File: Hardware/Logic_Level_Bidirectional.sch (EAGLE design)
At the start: 17 parts, among them Q1 BSS138, Q2 BSS138, Q3 BSS138, Q4 BSS138

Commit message: Updated Schematic Frame
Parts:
- removed CC_TEXT1: CREATIVE_COMMONS, SparkFun-Aesthetics:CREATIVE_COMMONS
- JP3, JP4: device SparkFun:FIDUCIALUFIDUCIAL -> SparkFun-Aesthetics:FIDUCIALUFIDUCIAL
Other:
- note added: "Patrick Alberts"
- note removed: "Nathan Seidle"
- note removed: "Rev V13 by Patrick Alberts"
- note removed: "Spark Fun Electronics"
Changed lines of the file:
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@@
 </classes>
 <parts>
-<part name="FRAME1" library="SparkFun" deviceset="FRAME-LETTER" device=""/>
 <part name="Q2" library="SparkFun" deviceset="MOSFET-NCHANNEL" device="SMD" value="BSS138"/>
 <part name="R6" library="SparkFun" deviceset="RESISTOR" device="0603-RES" value="10K"/>
@@
 <part name="JP1" library="SparkFun" deviceset="M06" device="SIP"/>
 <part name="JP2" library="SparkFun" deviceset="M06" device="SIP"/>
-<part name="JP3" library="SparkFun" deviceset="FIDUCIAL" device="UFIDUCIAL"/>
-<part name="JP4" library="SparkFun" deviceset="FIDUCIAL" device="UFIDUCIAL"/>
-<part name="CC_TEXT1" library="SparkFun-Aesthetics" deviceset="CREATIVE_COMMONS" device=""/>
 <part name="Q3" library="SparkFun" deviceset="MOSFET-NCHANNEL" device="SMD" value="BSS138"/>
 <part name="R2" library="SparkFun" deviceset="RESISTOR" device="0603-RES" value="10K"/>
@@
 <part name="P+5" library="SparkFun" deviceset="VCC" device="" value="LV"/>
 <part name="P+6" library="SparkFun" deviceset="VCC" device="" value="HV"/>
+<part name="FRAME1" library="SparkFun-Aesthetics" deviceset="FRAME-LETTER" device=""/>
+<part name="JP3" library="SparkFun-Aesthetics" deviceset="FIDUCIAL" device="UFIDUCIAL"/>
+<part name="JP4" library="SparkFun-Aesthetics" deviceset="FIDUCIAL" device="UFIDUCIAL"/>
 </parts>
 <sheets>
@@
 <wire x1="124.46" y1="185.42" x2="127" y2="185.42" width="0.2032" layer="95" style="longdash"/>
 <wire x1="127" y1="185.42" x2="127" y2="121.92" width="0.2032" layer="95" style="longdash"/>
-<text x="154.94" y="27.94" size="2.54" layer="94">Spark Fun Electronics</text>
 <text x="48.26" y="170.18" size="3.302" layer="95">Channel 1</text>
 <text x="175.26" y="170.18" size="3.302" layer="95">Channel 2</text>
 <text x="169.672" y="104.394" size="3.302" layer="95">High Voltage</text>
 <text x="50.546" y="105.41" size="3.302" layer="95">Low Voltage</text>
-<text x="17.78" y="5.08" size="1.778" layer="97" font="vector">Nathan Seidle </text>
-<text x="40.64" y="5.08" size="1.778" layer="97" font="vector">Rev V13 by Patrick Alberts</text>
-<text x="238.76" y="7.62" size="2.54" layer="94">V01</text>
+<text x="241.3" y="48.26" size="2.54" layer="94">V01</text>
+<text x="166.624" y="52.324" size="2.54" layer="94">Patrick Alberts</text>
 </plain>
 <instances>
-<instance part="FRAME1" gate="G$1" x="0" y="0"/>
-<instance part="FRAME1" gate="G$2" x="147.32" y="0"/>
 <instance part="Q2" gate="G$1" x="162.56" y="137.16" smashed="yes" rot="R270">
 <attribute name="NAME" x="158.75" y="141.986" size="1.778" layer="95"/>
@@
 <attribute name="VALUE" x="193.04" y="101.6" size="1.778" layer="96" rot="R180"/>
 </instance>
-<instance part="JP3" gate="G$1" x="205.74" y="27.94"/>
-<instance part="JP4" gate="G$1" x="205.74" y="33.02"/>
-<instance part="CC_TEXT1" gate="G$1" x="5.08" y="5.08"/>
 <instance part="Q3" gate="G$1" x="78.74" y="137.16" smashed="yes" rot="R270">
 <attribute name="NAME" x="74.93" y="141.986" size="1.778" layer="95"/>
@@
 <instance part="P+5" gate="1" x="198.12" y="154.94"/>
 <instance part="P+6" gate="1" x="213.36" y="154.94"/>
+<instance part="FRAME1" gate="G$1" x="0" y="40.64"/>
+<instance part="FRAME1" gate="G$2" x="147.32" y="40.64"/>
+<instance part="JP3" gate="G$1" x="243.84" y="73.66"/>
+<instance part="JP4" gate="G$1" x="243.84" y="68.58"/>
 </instances>
 <busses>

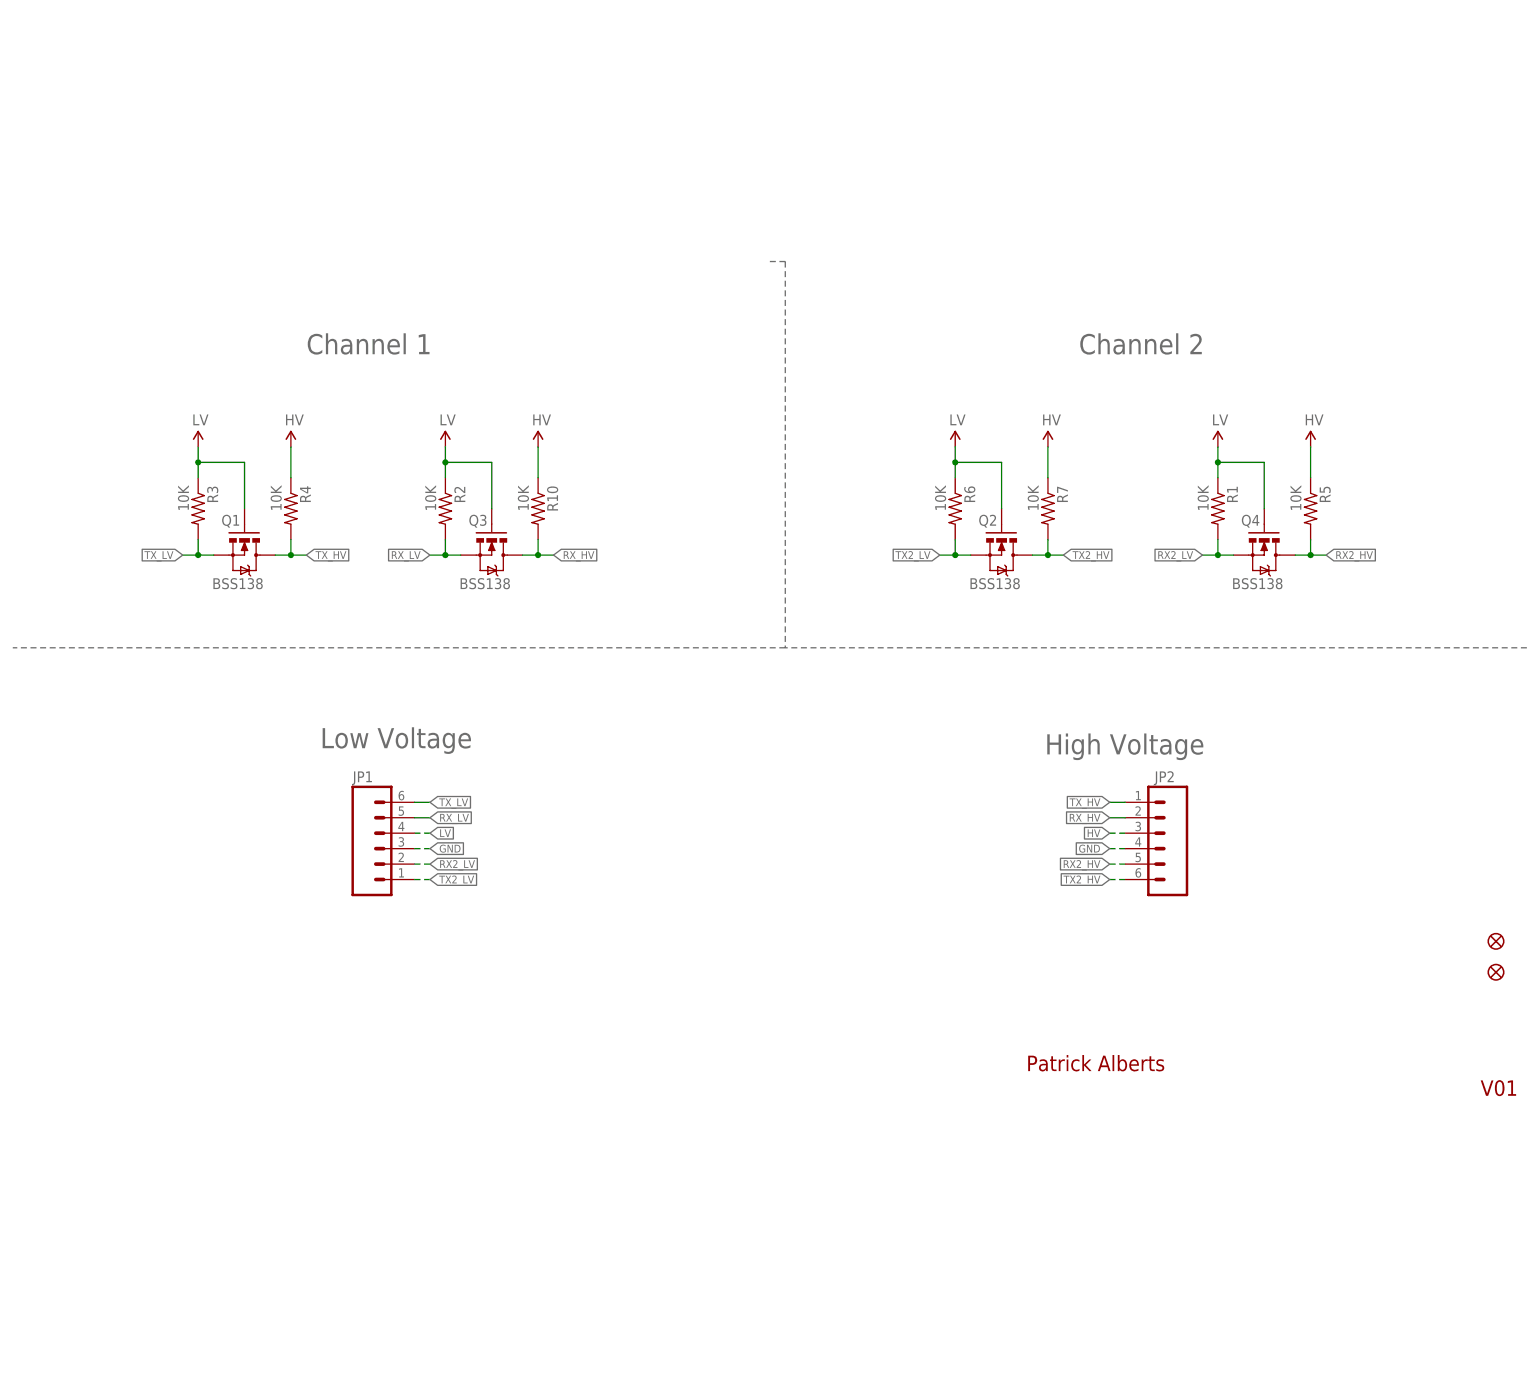
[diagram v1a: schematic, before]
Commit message: Silk Change, Schematic Change
Added deviding lines for HV/LV passages and change silk names as well
from RXO/TXO to HV1 LV2...etc as well as cleaned up the schematic.
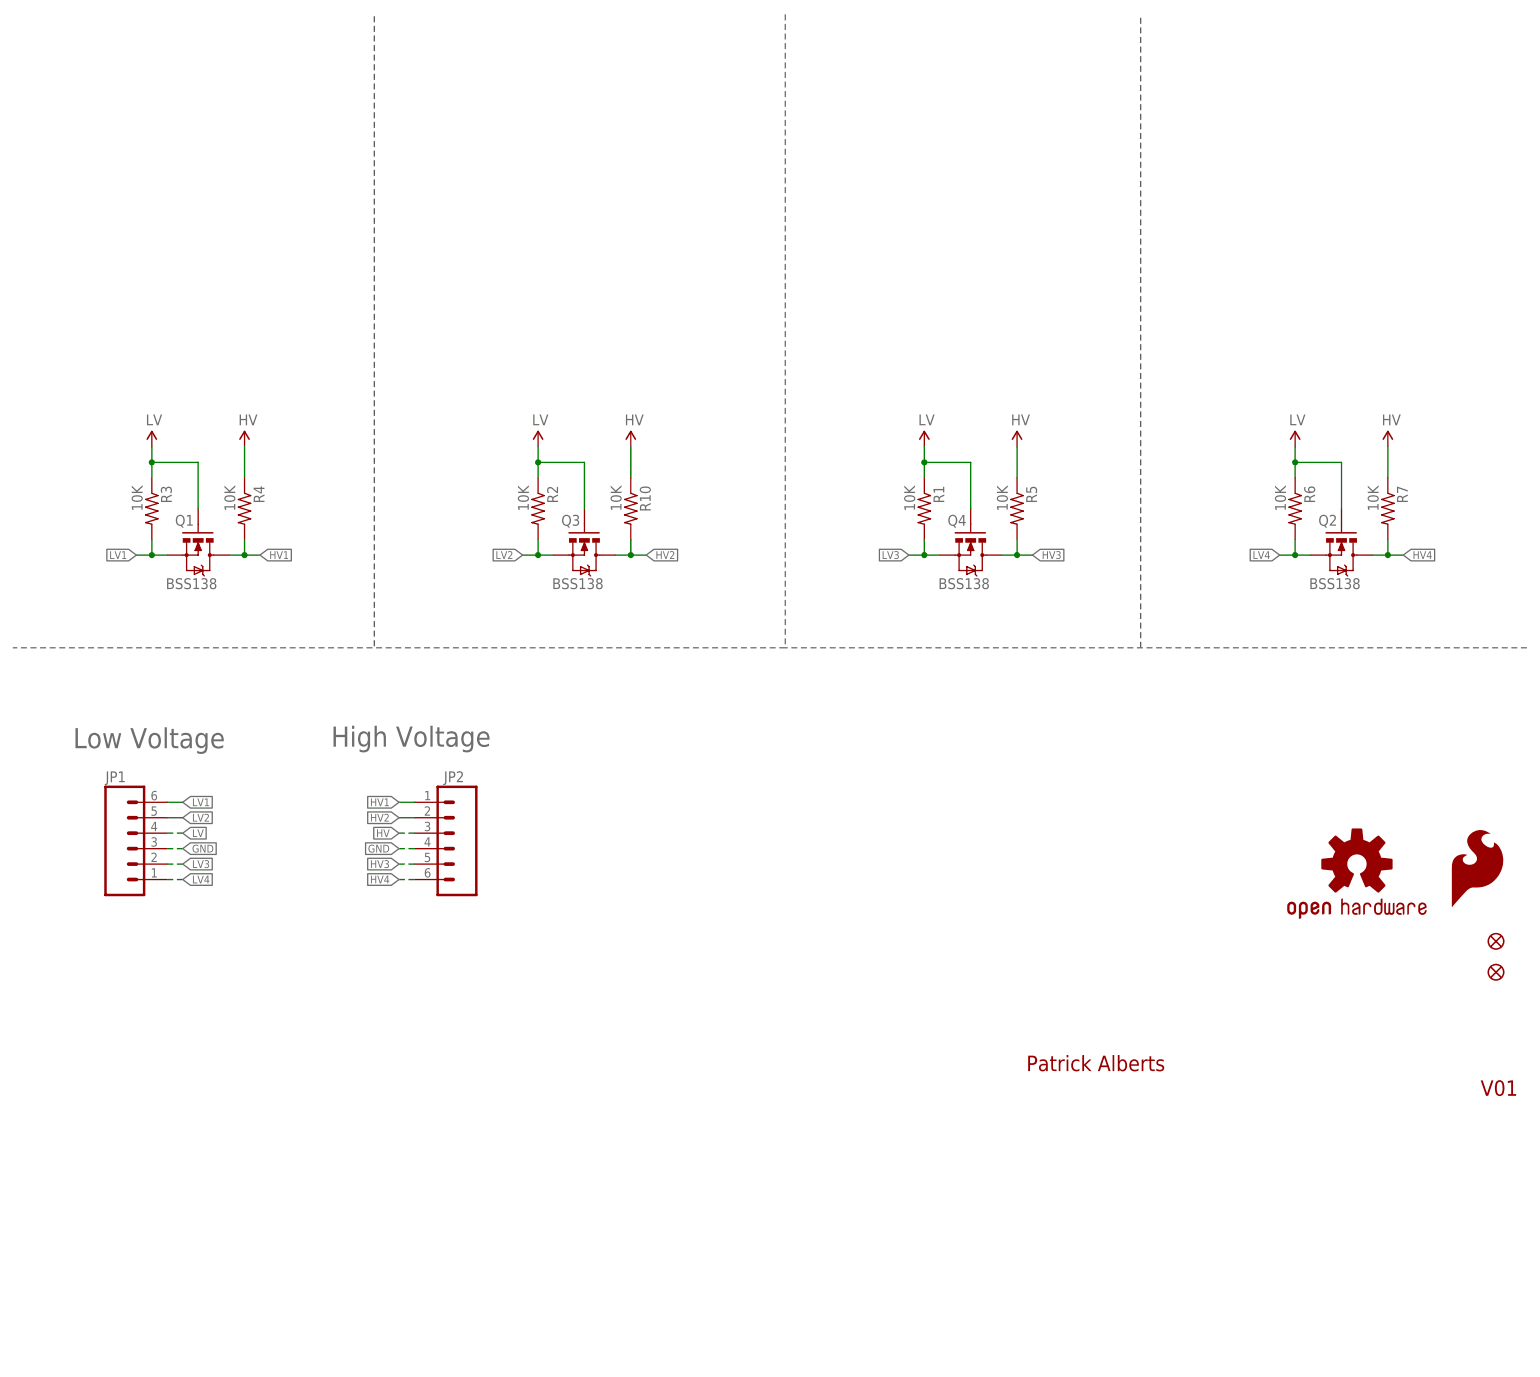
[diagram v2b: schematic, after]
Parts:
- added LOGO1: SFE_LOGO_FLAME.1_INCH, SparkFun-Aesthetics:SFE_LOGO_FLAME.1_INCH
- added LOGO2: OSHW-LOGOS, SparkFun-Aesthetics:OSHW-LOGOS
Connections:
- net RX2_HV renamed HV3
- net RX2_LV renamed LV3
- net RX_HV renamed HV2
- net RX_LV renamed LV2
- net TX2_HV renamed HV4
- net TX2_LV renamed LV4
- net TX_HV renamed HV1
- net TX_LV renamed LV1
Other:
- note removed: "Channel 1"
- note removed: "Channel 2"
- moved on the sheet: JP1, JP2, Q1, Q2, Q3, Q4, R1, R10, R2, R3, R4, R5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
